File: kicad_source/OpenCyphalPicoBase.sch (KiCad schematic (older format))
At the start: 30 parts, among them CN1 RASPBERRYPI_PICO, CN2 SM04B-SRSS-TB, CN3 SM04B-SRSS-TB, CN6 691322310002, CN7 CONN_02X03, CN8 WAGO 733-362, U3 24LC64

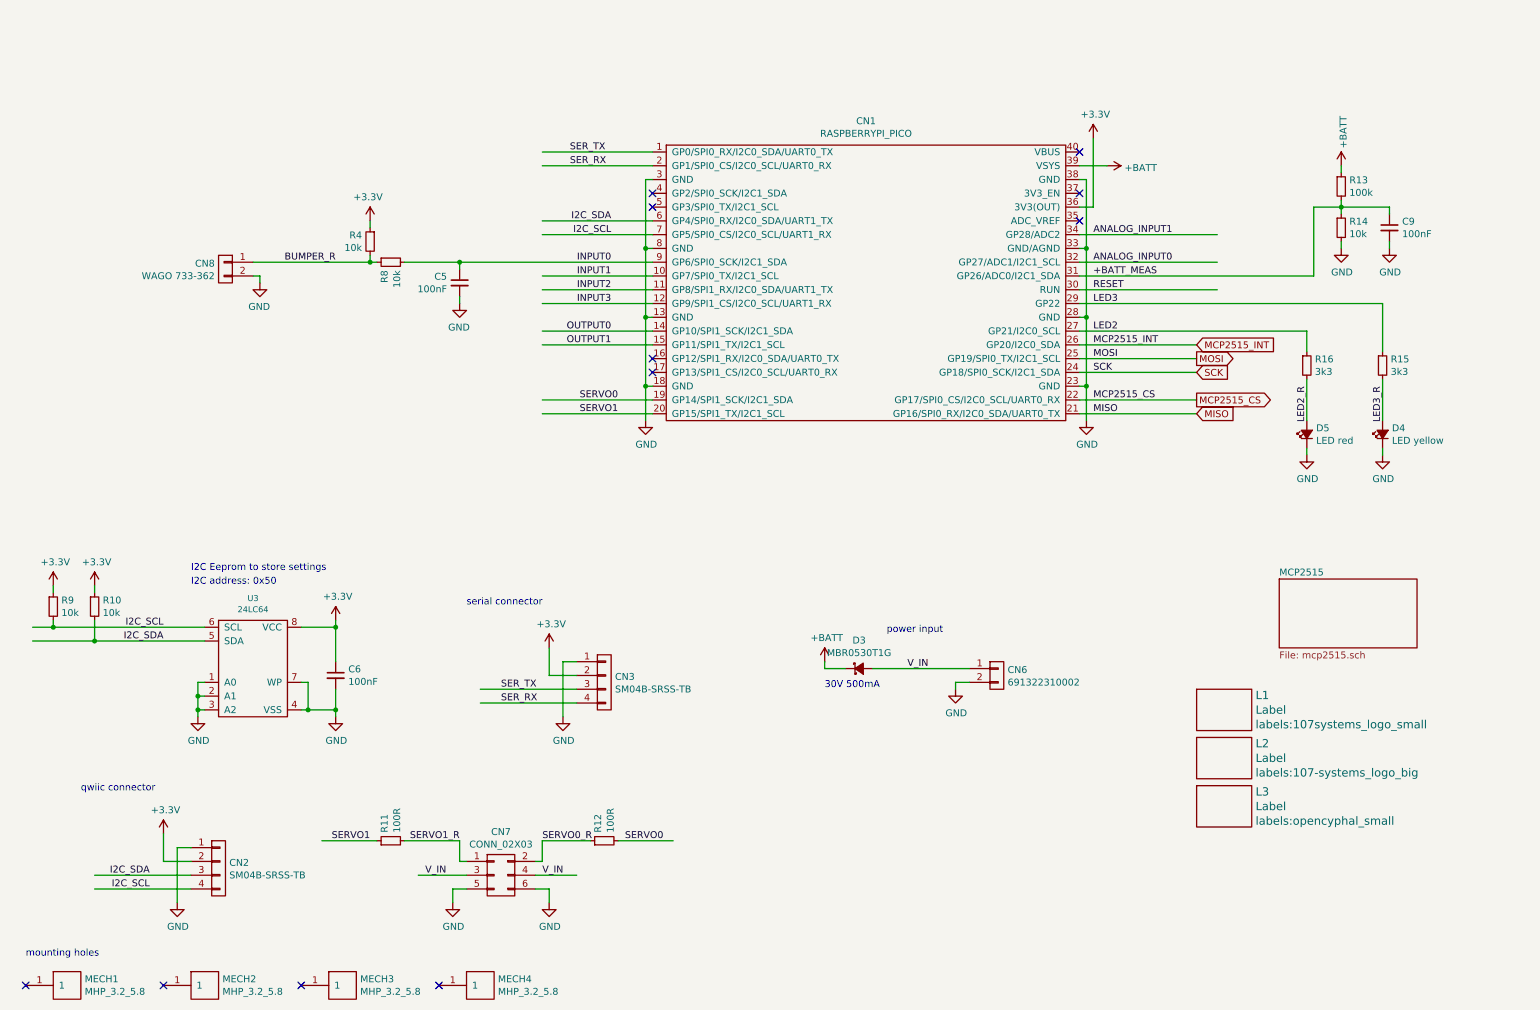
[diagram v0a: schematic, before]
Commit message: updated layout, added connectors for input and output
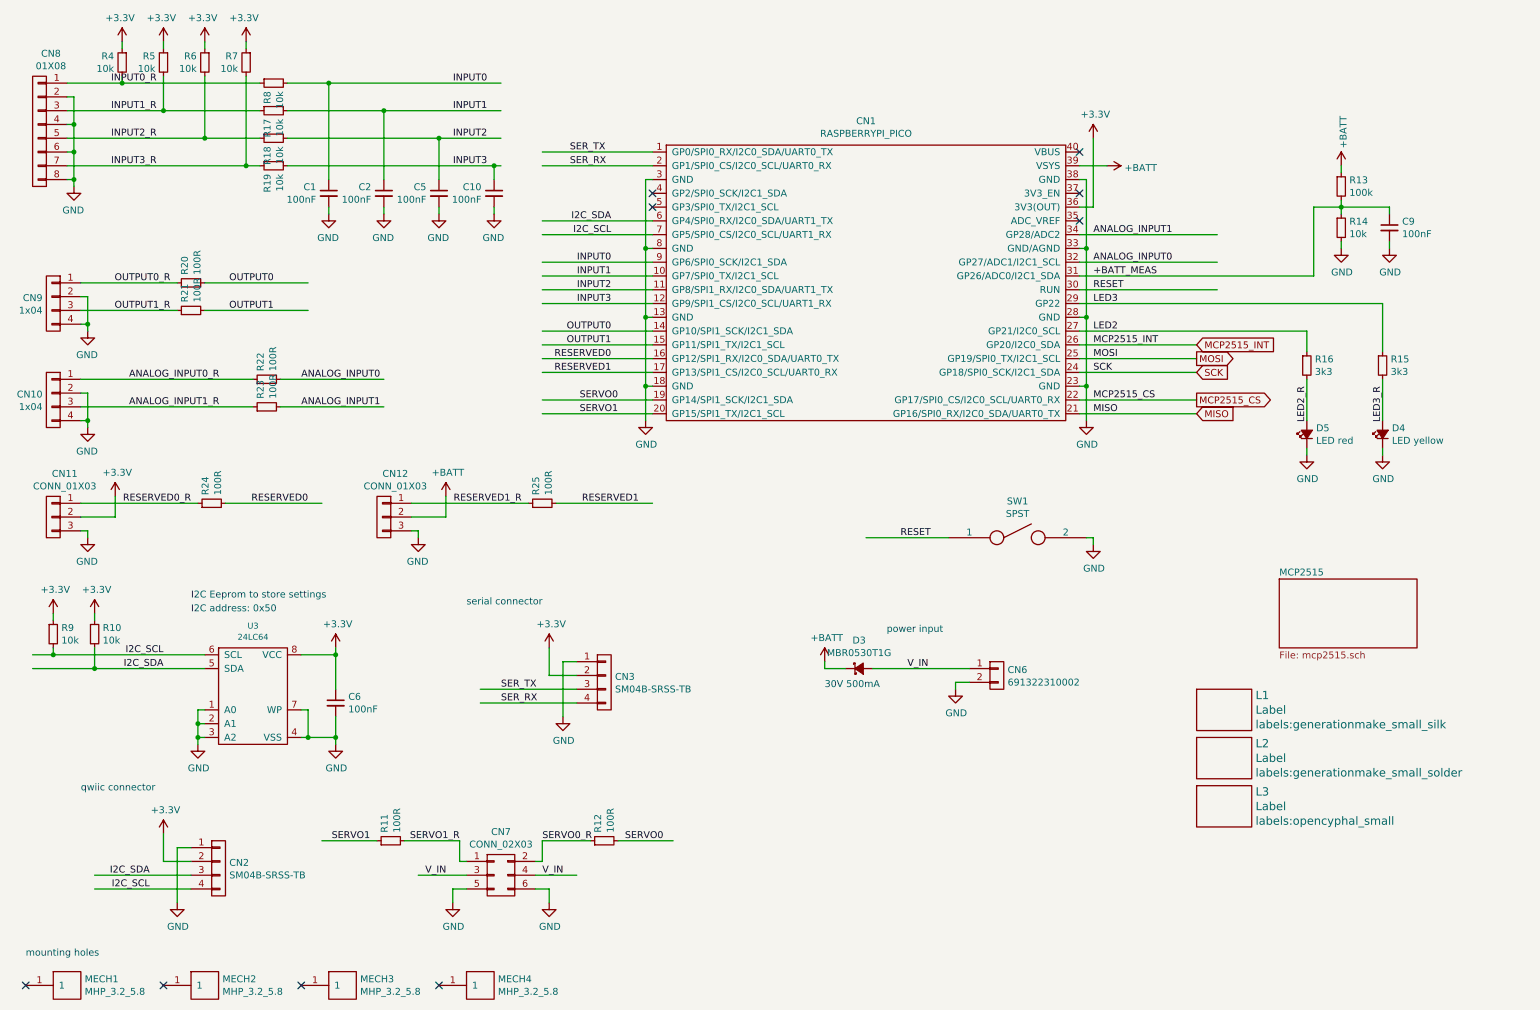
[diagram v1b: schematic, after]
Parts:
- removed CN8: WAGO 733-362, CON_wuerth:WR-TBL_691382010002, symbol mechanical-connectors:CONN_01X02
- added C1, C10, C2: 100nF, capacitors:C_0603, symbol devices:C_0603
- added CN10, CN9: 1x04, pin_headers:Pin_Header_Straight_1x04, symbol mechanical-connectors:CONN_01X04
- added CN11, CN12: CONN_01X03, pin_headers:Pin_Header_Straight_1x03, symbol mechanical-connectors:CONN_01X03
- added CN8: 01X08, pin_headers:Pin_Header_Straight_1x08, symbol mechanical-connectors:CONN_01X08
- added R17, R18, R19, R5, R6, R7: 10k, resistors:R_0603, symbol devices:R_0603
- added R20, R21, R22, R23, R24, R25: 100R, resistors:R_0603, symbol devices:R_0603
- added SW1: SPST, mechanical-switches:WE_434121050816, symbol devices:SPST
- L1: footprint labels:107systems_logo_small -> labels:generationmake_small_silk
- L2: footprint labels:107-systems_logo_big -> labels:generationmake_small_solder
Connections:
- net labels added: ANALOG_INPUT0_R, ANALOG_INPUT1_R, INPUT0_R, INPUT1_R, INPUT2_R, INPUT3_R, OUTPUT0_R, OUTPUT1_R, RESERVED0, RESERVED0_R, RESERVED1, RESERVED1_R
- net labels removed: BUMPER_R
- wire segments 120 -> 184
- no-connect marks 11 -> 9
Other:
- moved on the sheet: C6, R10, R9, U3

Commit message: added solder pads for raspberry pi pico
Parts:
- CN1: footprint MODULE_compute:RASPI_PICO -> MODULE_compute:RASPI_PICO_SOLDER
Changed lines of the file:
@@
 F 0 "CN1" H 6800 3675 50  0000 C CNN
 F 1 "RASPBERRYPI_PICO" H 6800 3584 50  0000 C CNN
-F 2 "MODULE_compute:RASPI_PICO" H 6800 2500 50  0001 C CNN
+F 2 "MODULE_compute:RASPI_PICO_SOLDER" H 6800 2500 50  0001 C CNN
 F 3 "" H 6800 2500 50  0001 C CNN
 	1    6800 2500
